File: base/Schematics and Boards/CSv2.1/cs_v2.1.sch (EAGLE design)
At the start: 77 parts, among them J101 J-JTAG-CORTEX-NEEDLE6-LEGS, J301 HIROSE-DF40_50-PIN_CONNECTORS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, J302 HIROSE-DF40_50-PIN_CONNECTORS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, Q1 DMG3415UFY4Q-7F, U1 NCP708MU330TAG, U101 ATSAMD51, U2 W25N01GVZEIG, U201 COULOMB-MAX17262, U202 MAX77827BEWC+T, U203 SENSOR-SI7006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

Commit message: Update files per design review and regenerate CAM
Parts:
- added R3: 100k, Resistors:R-0402
- R101: MPN (none) -> ERJ-2GEJ103X
- R207: value 0.51 -> 0.24; MANUFACTURER Ohmite -> (none); MPN KDV06DR510ET -> ERJ-2BQFR24X; PART_NO KDV06DR510ET -> ERJ-2BQFR24X
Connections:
- net +3V3_STOR: now also R3.1
- net STOR_QSPI_CS: now also R3.2
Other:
- note added: "128MB capacity"
- note added: "Aim for 1 mA output for each LED. Green (1) and Blue(3) have forward biases near 3V Red (2) has forward bias 1.8V. Outputs of this should be tied to GND by processor to turn an LED on."
- note added: "Max CLK Rate: 104MHz"
- note added: "Status register 1, bit WP-E, SRP1/0 will set options for Quad SPI and othe basic options"
- note added: "Switch has 260-350 mΩ resistance Estimate typical 260 mΩ for total 0.5Ω to account for ~200mA of current"
- note removed: "Aim for 1 mA output for each LED. Green (1) and Blue(3) have forward biases near 3V, so no resistor needed. Red (2) has forward bias 1.8V. Outputs of this should be tied to GND by processor to turn an LED on."
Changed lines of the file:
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@@
 <part name="GND7" library="Supplies" deviceset="GND" device=""/>
 <part name="R101" library="Resistors" deviceset="R-" device="0402" value="10k">
+<attribute name="MPN" value="ERJ-2GEJ103X"/>
 <attribute name="PART_NO" value="ERJ-2GEJ103X"/>
 </part>
@@
 <attribute name="TOL" value="0.1%"/>
 </part>
-<part name="R207" library="Resistors" deviceset="R-" device="0603" value="0.51">
-<attribute name="MANUFACTURER" value="Ohmite"/>
-<attribute name="MPN" value="KDV06DR510ET"/>
-<attribute name="PART_NO" value="KDV06DR510ET"/>
+<part name="R207" library="Resistors" deviceset="R-" device="0603" value="0.24">
+<attribute name="MPN" value="ERJ-2BQFR24X"/>
+<attribute name="PART_NO" value="ERJ-2BQFR24X"/>
 <attribute name="TOL" value="0.5%"/>
 </part>
@@
 <attribute name="PART_NO" value="DMG3415U-7"/>
 </part>
+<part name="R3" library="Resistors" deviceset="R-" device="0402" value="100k">
+<attribute name="MPN" value="ERJ-2GEJ104X"/>
+<attribute name="PART_NO" value="ERJ-2GEJ104X"/>
+</part>
 </parts>
 <sheets>
@@
 <text x="231.14" y="226.06" size="2.54" layer="91">I2C Pull-ups</text>
 <text x="302.26" y="119.38" size="3.81" layer="91">External FLASH Storage</text>
+<text x="373.38" y="114.3" size="1.778" layer="91">128MB capacity</text>
+<text x="327.66" y="76.2" size="1.778" layer="91">Max CLK Rate: 104MHz</text>
+<text x="302.26" y="53.34" size="1.778" layer="91">Status register 1, bit WP-E, SRP1/0 will set
+ options for Quad SPI and othe basic options</text>
 </plain>
 <instances>
@@
 <attribute name="VALUE" x="186.182" y="212.09" size="1.778" layer="96" rot="R90"/>
 <attribute name="PART_NO" x="182.88" y="215.9" size="1.778" layer="96" rot="R90" display="off"/>
+<attribute name="MPN" x="182.88" y="215.9" size="1.778" layer="96" rot="R90" display="off"/>
 </instance>
 <instance part="R102" gate="G$1" x="198.12" y="208.28" smashed="yes">
@@
 <attribute name="NAME" x="350.6216" y="109.1946" size="2.0828" layer="95" ratio="6" rot="SR0"/>
 <attribute name="VALUE" x="350.4946" y="106.6546" size="2.0828" layer="96" ratio="6" rot="SR0"/>
+</instance>
+<instance part="R3" gate="G$1" x="350.52" y="114.3" smashed="yes" rot="R180">
+<attribute name="NAME" x="354.33" y="112.8014" size="1.778" layer="95" rot="R180"/>
+<attribute name="VALUE" x="354.33" y="117.602" size="1.778" layer="96" rot="R180"/>
+<attribute name="PART_NO" x="350.52" y="114.3" size="1.778" layer="96" rot="R180" display="off"/>
+<attribute name="MPN" x="350.52" y="114.3" size="1.778" layer="96" rot="R180" display="off"/>
 </instance>
 </instances>
@@
 <net name="+3V3_STOR" class="1">
 <segment>
-<wire x1="365.76" y1="111.76" x2="365.76" y2="114.3" width="0.1524" layer="91"/>
 <pinref part="+3V9" gate="G$1" pin="+3V3"/>
 <label x="365.76" y="124.46" size="1.778" layer="95"/>
 <pinref part="U2" gate="A" pin="VCC"/>
 <wire x1="365.76" y1="114.3" x2="365.76" y2="119.38" width="0.1524" layer="91"/>
-<wire x1="365.76" y1="109.22" x2="365.76" y2="111.76" width="0.1524" layer="91"/>
+<wire x1="365.76" y1="109.22" x2="365.76" y2="114.3" width="0.1524" layer="91"/>
+<wire x1="355.6" y1="114.3" x2="365.76" y2="114.3" width="0.1524" layer="91"/>
+<junction x="365.76" y="114.3"/>
+<pinref part="R3" gate="G$1" pin="1"/>
 </segment>
 </net>
@@
 <pinref part="U2" gate="A" pin="/CS"/>
 <wire x1="294.64" y1="86.36" x2="297.18" y2="83.82" width="0.1524" layer="91"/>
-<wire x1="297.18" y1="83.82" x2="350.52" y2="83.82" width="0.1524" layer="91"/>
+<wire x1="297.18" y1="83.82" x2="345.44" y2="83.82" width="0.1524" layer="91"/>
 <label x="320.04" y="83.82" size="1.778" layer="95"/>
+<wire x1="345.44" y1="83.82" x2="350.52" y2="83.82" width="0.1524" layer="91"/>
+<wire x1="345.44" y1="83.82" x2="345.44" y2="114.3" width="0.1524" layer="91"/>
+<junction x="345.44" y="83.82"/>
+<pinref part="R3" gate="G$1" pin="2"/>
 </segment>
 </net>
@@
 <text x="198.12" y="86.36" size="2.54" layer="91">Buck-boost</text>
 <text x="15.24" y="12.7" size="1.778" layer="91">Aim for 1 mA output for each LED.
-Green (1) and Blue(3) have forward biases near 3V,
-so no resistor needed.
+Green (1) and Blue(3) have forward biases near 3V
 Red (2) has forward bias 1.8V.
 Outputs of this should be tied to GND by
@@
   because low-profile switches with &gt;0.5A
   are seemingly impossible to find.</text>
-<text x="269.24" y="208.28" size="1.778" layer="91">Replace sense resisitor with 0Ω
+<text x="269.24" y="223.52" size="1.778" layer="91">Replace sense resisitor with 0Ω
   for designs where power is essential</text>
 <text x="269.24" y="139.7" size="1.778" layer="91">Replace sense resisitor with 0Ω
   for designs where power is essential</text>
 <text x="337.82" y="162.56" size="1.778" layer="91">Switch has 300-500 mΩ resistance!</text>
+<text x="292.354" y="205.74" size="1.778" layer="91">Switch has 260-350 mΩ resistance
+Estimate typical 260 mΩ for total 0.5Ω
+to account for ~200mA of current</text>
 </plain>
 <instances>
@@
 </instance>
 <instance part="J302" gate="G$1" x="289.56" y="149.86" smashed="yes" rot="R90">
-<attribute name="NAME" x="265.9166" y="142.21801875" size="1.273659375" layer="95" rot="R90"/>
+<attribute name="NAME" x="255.7566" y="147.29801875" size="1.273659375" layer="95" rot="R90"/>
 <attribute name="PART_NO" x="289.56" y="149.86" size="1.778" layer="96" rot="R90" display="off"/>
 <attribute name="MPN" x="289.56" y="149.86" size="1.778" layer="96" rot="R90" display="off"/>

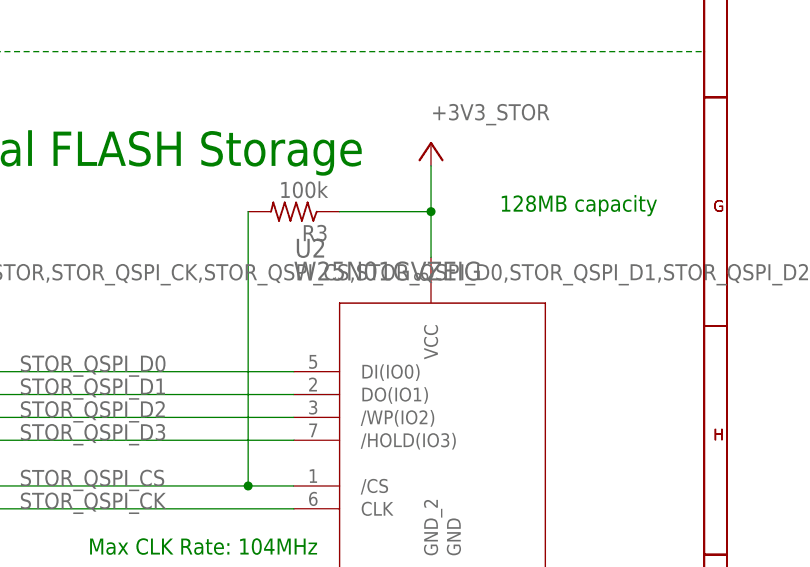
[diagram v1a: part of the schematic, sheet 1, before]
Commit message: Minor part renaming per octopart BOM tool
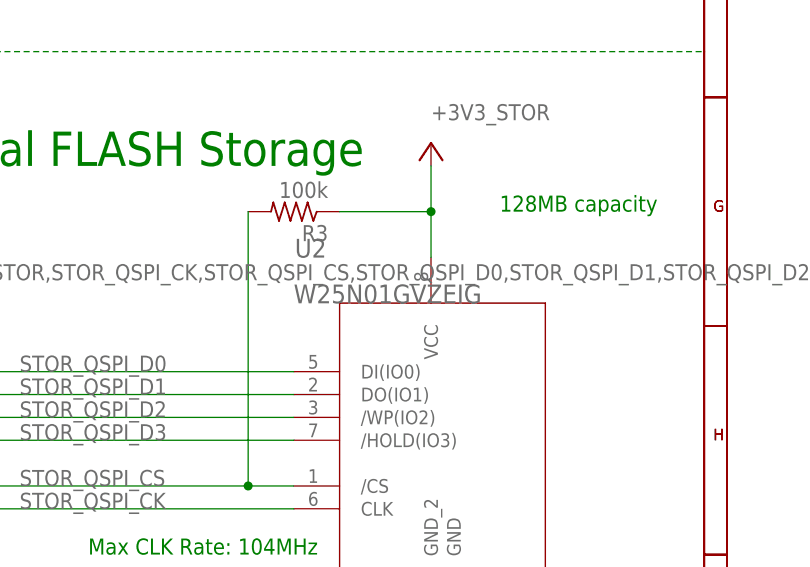
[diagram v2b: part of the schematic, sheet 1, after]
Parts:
- U2: MANUFACTURER_PART_NUMBER (none) -> W25N01GVZEIG TR; MP (none) -> W25N01GVZEIG TR; MPN (none) -> W25N01GVZEIG TR; PART_NO (none) -> W25N01GVZEIG TR
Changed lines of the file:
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@@
 <part name="GND6" library="Supplies" deviceset="GND" device=""/>
 <part name="U1" library="Regulators" deviceset="LDO_ONSEMI_NCP708" device="" value="NCP708MU330TAG"/>
-<part name="U2" library="Storage" deviceset="W25N01GVZEIG" device=""/>
+<part name="U2" library="Storage" deviceset="W25N01GVZEIG" device="">
+<attribute name="MANUFACTURER_PART_NUMBER" value="W25N01GVZEIG TR"/>
+<attribute name="MP" value="W25N01GVZEIG TR"/>
+<attribute name="MPN" value="W25N01GVZEIG TR"/>
+<attribute name="PART_NO" value="W25N01GVZEIG TR"/>
+</part>
 <part name="U3" library="Switches" deviceset="TS3A24159YZPR" device="">
 <attribute name="MP" value="TS3A24159YZPR"/>
@@
 <instance part="U2" gate="A" x="365.76" y="88.9" smashed="yes">
 <attribute name="NAME" x="350.6216" y="109.1946" size="2.0828" layer="95" ratio="6" rot="SR0"/>
-<attribute name="VALUE" x="350.4946" y="106.6546" size="2.0828" layer="96" ratio="6" rot="SR0"/>
+<attribute name="VALUE" x="350.4946" y="104.1146" size="2.0828" layer="96" ratio="6" rot="SR0"/>
 </instance>
 <instance part="R3" gate="G$1" x="350.52" y="114.3" smashed="yes" rot="R180">
